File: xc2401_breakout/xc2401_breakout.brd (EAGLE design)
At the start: 25.4 x 25.4 mm, 11 parts, among them U1 XC2401

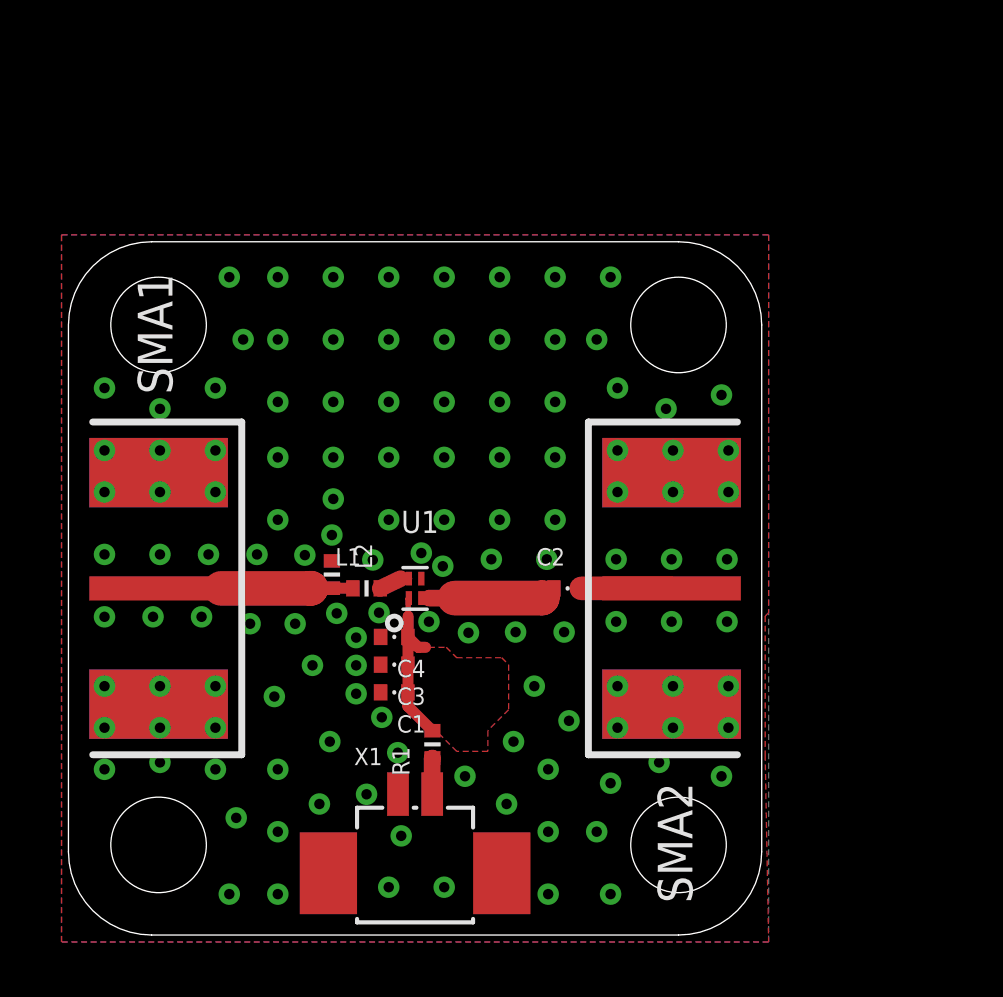
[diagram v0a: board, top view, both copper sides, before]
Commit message: Changed board dims to 1.25x1.25 in for barebones specs Added more bare area around holes
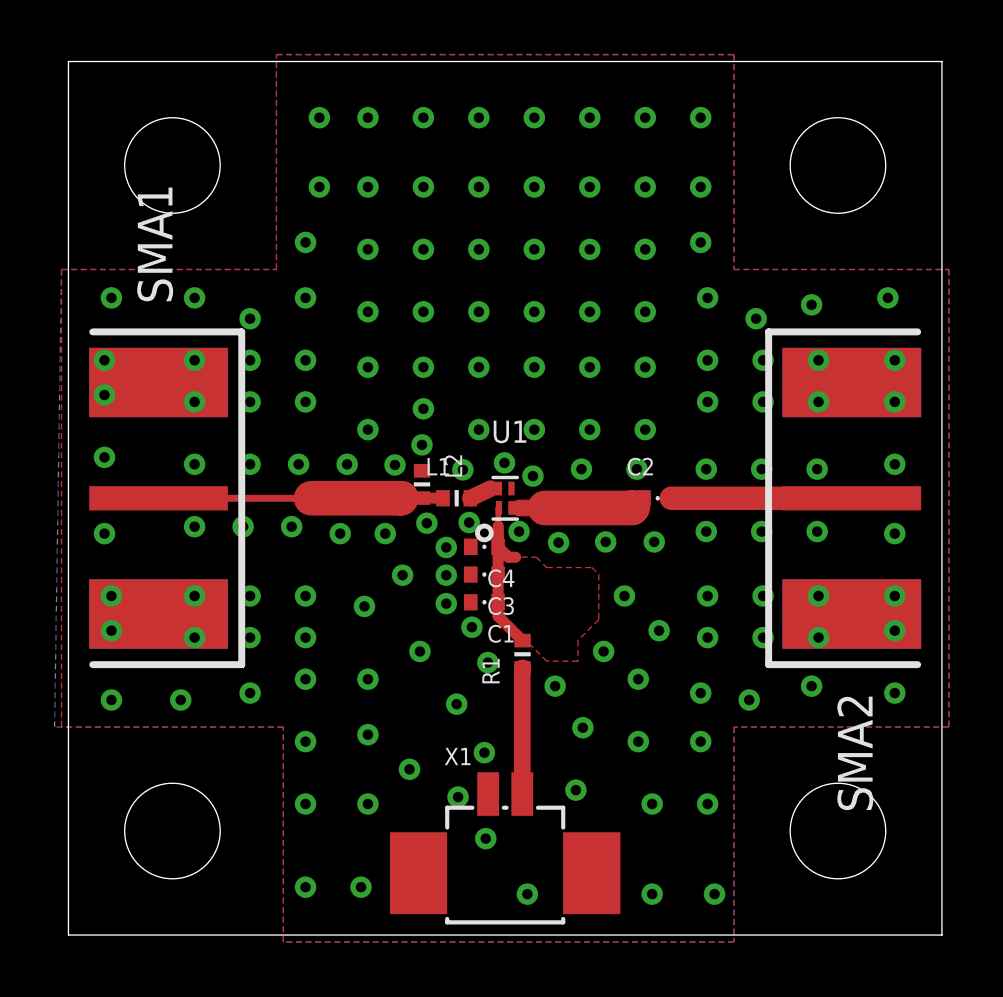
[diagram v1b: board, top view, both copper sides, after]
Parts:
- moved SMA2 7.38 mm to (31.2, 16.0)
- moved L2 4.67 mm to (13.0, 16.5)
- moved R1 4.67 mm to (16.6, 10.3)
- moved C1 4.67 mm to (15.2, 12.2)
- moved C2 4.67 mm to (21.6, 16.0)
- moved C3 4.67 mm to (15.2, 13.2)
- moved C4 4.67 mm to (15.2, 14.2)
- moved L1 4.67 mm to (14.2, 16.0)
- moved U1 4.67 mm to (16.0, 16.0)
- moved SMA1 3.30 mm to (0.76, 16.0)
- moved X1 3.30 mm to (16.0, 4.06)
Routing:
- net N$4: track 7.13 -> 10.4 mm
- net N$3: track 3.31 -> 6.61 mm
- net N$6: track 1.33 -> 4.63 mm
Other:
- board size 25.4 x 25.4 mm -> 32 x 32 mm

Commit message: Forgot to lengthen transmission lines
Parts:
- moved C2 3.56 mm to (25.1, 16.0)
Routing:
- net N$2: track 5.01 -> 9.01 mm
- net N$3: track 6.61 -> 3.06 mm
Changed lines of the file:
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@@
 <element name="C1" library="pel_dipol_comp" package="0402-CAP" value="10nF" x="15.24" y="12.192" rot="R180"/>
 <element name="R1" library="pel_dipol_comp" package="0402-RES" value="600" x="16.637" y="10.287" rot="R90"/>
-<element name="C2" library="pel_dipol_comp" package="0402-CAP" value="100pF" x="21.59" y="16.002"/>
+<element name="C2" library="pel_dipol_comp" package="0402-CAP" value="100pF" x="25.146" y="16.002"/>
 <element name="L1" library="pel_dipol_comp" package="0402-IND" value="6.2nH" x="14.224" y="16.002"/>
 <element name="L2" library="pel_dipol_comp" package="0402-IND" value="9.1nH" x="12.954" y="16.51" rot="R270"/>
@@
 <via x="15.9766" y="17.2974" extent="1-16" drill="0.381"/>
 <via x="17.018" y="16.8148" extent="1-16" drill="0.381"/>
-<via x="6.6548" y="17.2466" extent="1-16" drill="0.381"/>
-<via x="4.6228" y="17.2466" extent="1-16" drill="0.381"/>
+<via x="5.8928" y="17.2466" extent="1-16" drill="0.381"/>
+<via x="3.8608" y="17.2466" extent="1-16" drill="0.381"/>
 <via x="9.9568" y="14.7066" extent="1-16" drill="0.381"/>
-<via x="6.4008" y="14.9606" extent="1-16" drill="0.381"/>
-<via x="4.6228" y="14.9606" extent="1-16" drill="0.381"/>
+<via x="6.1468" y="14.7066" extent="1-16" drill="0.381"/>
+<via x="3.8608" y="14.9606" extent="1-16" drill="0.381"/>
 <via x="18.796" y="17.0688" extent="1-16" drill="0.381"/>
 <via x="20.828" y="17.0688" extent="1-16" drill="0.381"/>
@@
 <via x="19.685" y="14.4018" extent="1-16" drill="0.381"/>
 <via x="21.463" y="14.4018" extent="1-16" drill="0.381"/>
-<via x="23.368" y="14.7828" extent="1-16" drill="0.381"/>
+<via x="23.622" y="14.2748" extent="1-16" drill="0.381"/>
 <via x="25.4" y="14.7828" extent="1-16" drill="0.381"/>
-<via x="27.432" y="14.7828" extent="1-16" drill="0.381"/>
-<via x="27.432" y="17.0688" extent="1-16" drill="0.381"/>
+<via x="27.94" y="14.7828" extent="1-16" drill="0.381"/>
+<via x="27.94" y="17.0688" extent="1-16" drill="0.381"/>
 <via x="25.4" y="17.0688" extent="1-16" drill="0.381"/>
-<via x="23.368" y="17.0688" extent="1-16" drill="0.381"/>
+<via x="23.114" y="17.0688" extent="1-16" drill="0.381"/>
 <polygon width="0.254" layer="16">
 <vertex x="-0.254" y="24.384"/>
@@
 <via x="19.6088" y="10.3886" extent="1-16" drill="0.381"/>
 <via x="18.8468" y="7.5946" extent="1-16" drill="0.381"/>
-<via x="8.4328" y="17.2466" extent="1-16" drill="0.381"/>
-<via x="8.1788" y="14.9606" extent="1-16" drill="0.381"/>
+<via x="8.1788" y="17.2466" extent="1-16" drill="0.381"/>
+<via x="8.1788" y="14.7066" extent="1-16" drill="0.381"/>
 <via x="12.2428" y="13.1826" extent="1-16" drill="0.381"/>
 <via x="12.8778" y="10.3886" extent="1-16" drill="0.381"/>
@@
 <via x="1.5748" y="11.1506" extent="1-16" drill="0.381"/>
 <via x="1.5748" y="12.4206" extent="1-16" drill="0.381"/>
-<via x="1.3208" y="14.7066" extent="1-16" drill="0.381"/>
-<via x="1.3208" y="17.5006" extent="1-16" drill="0.381"/>
+<via x="1.3208" y="14.9606" extent="1-16" drill="0.381"/>
+<via x="1.3208" y="17.2466" extent="1-16" drill="0.381"/>
 <via x="1.3208" y="19.7866" extent="1-16" drill="0.381"/>
 <via x="1.3208" y="21.0566" extent="1-16" drill="0.381"/>
@@
 <wire x1="16.2306" y1="15.6464" x2="16.51" y2="15.6464" width="0.2032" layer="1"/>
 <wire x1="16.51" y1="15.6464" x2="17.4498" y2="15.6464" width="0.6096" layer="1"/>
-<wire x1="17.4498" y1="15.6464" x2="20.6502" y2="15.6464" width="1.27" layer="1"/>
-<wire x1="20.6502" y1="15.6464" x2="20.6756" y2="15.6718" width="1.27" layer="1"/>
-<wire x1="20.6756" y1="15.6718" x2="20.7598" y2="15.6718" width="0.254" layer="1"/>
-<wire x1="20.7598" y1="15.6718" x2="21.09" y2="16.002" width="0.254" layer="1"/>
+<wire x1="17.4498" y1="15.6464" x2="24.2062" y2="15.6464" width="1.27" layer="1"/>
+<wire x1="24.2062" y1="15.6464" x2="23.9776" y2="15.6718" width="1.27" layer="1"/>
+<wire x1="23.9776" y1="15.6718" x2="24.3158" y2="15.6718" width="0.254" layer="1"/>
+<wire x1="24.3158" y1="15.6718" x2="24.646" y2="16.002" width="0.254" layer="1"/>
 </signal>
 <signal name="N$3">
 <contactref element="C2" pad="P$2"/>
 <contactref element="SMA2" pad="P1"/>
-<wire x1="22.09" y1="16.002" x2="28.702" y2="16.002" width="0.8636" layer="1"/>
+<wire x1="25.646" y1="16.002" x2="28.702" y2="16.002" width="0.8636" layer="1"/>
 </signal>
 <signal name="N$4">
@@
 <wire x1="12.954" y1="16.01" x2="13.716" y2="16.01" width="0.4064" layer="1"/>
 <wire x1="13.716" y1="16.01" x2="13.724" y2="16.002" width="0.4064" layer="1"/>
-<wire x1="3.302" y1="16.002" x2="8.89" y2="16.002" width="0.254" layer="1"/>
-<wire x1="8.89" y1="16.002" x2="12.184" y2="16.002" width="1.27" layer="1"/>
+<wire x1="3.302" y1="16.002" x2="6.35" y2="16.002" width="0.254" layer="1"/>
+<wire x1="6.35" y1="16.002" x2="12.184" y2="16.002" width="1.27" layer="1"/>
 <wire x1="12.184" y1="16.002" x2="12.192" y2="16.01" width="1.27" layer="1"/>
 </signal>
